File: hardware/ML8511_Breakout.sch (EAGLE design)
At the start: 9 parts, among them U1 ML8511-UV-SENSOR

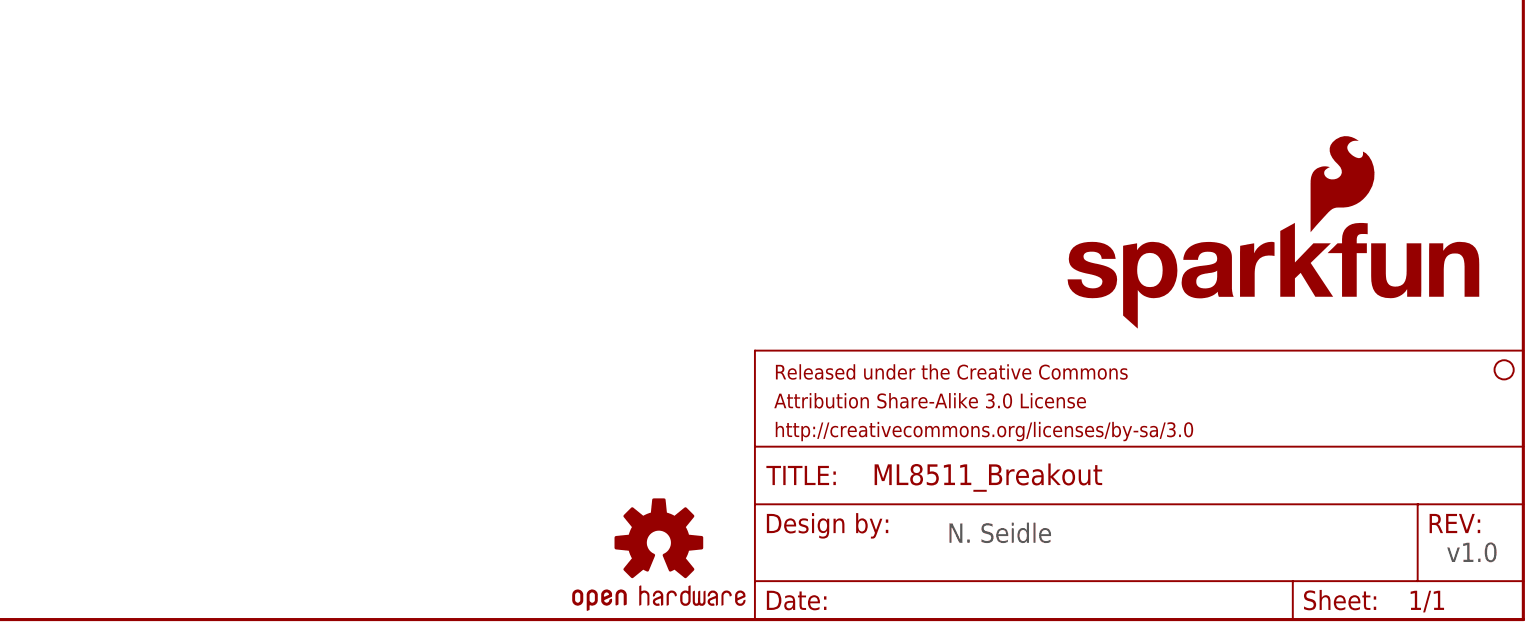
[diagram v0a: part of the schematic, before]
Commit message: DFM Changes
1.) Modified 3.3V trace so junction is not on IC pad
2.) Added trestrict under IC
3.) Routed GND trace directly away from IC
4.) Modified silk to better incorporate OSHW logo
5.) Version numbers between sch and brd are now consistent at v10
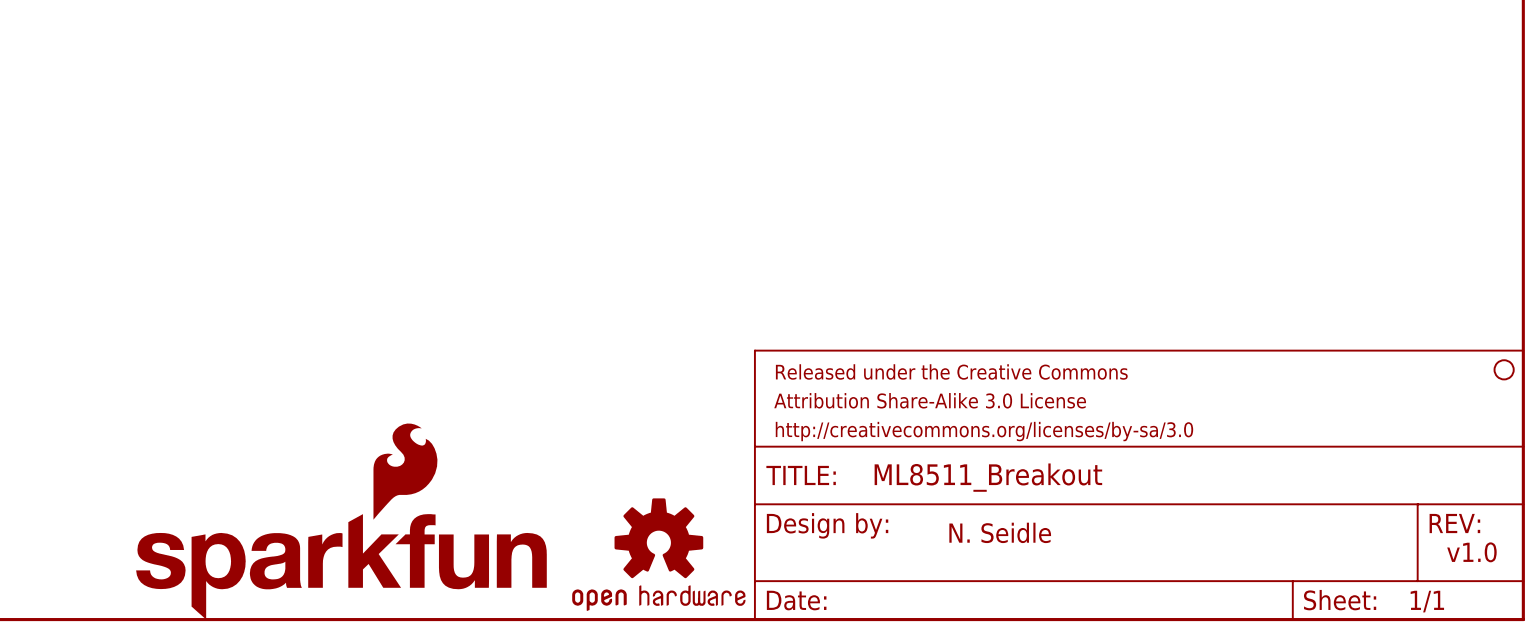
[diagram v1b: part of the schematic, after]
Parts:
- removed LOGO1: SFE_LOGO_NAME_FLAME.1_INCH, SparkFun-Aesthetics:SFE_LOGO_NAME_FLAME.1_INCH
- added LOGO3: SFE_LOGO_FLAME.1_INCH, SparkFun-Aesthetics:SFE_LOGO_FLAME.1_INCH
- added LOGO4: SFE_LOGO_NAME.1_INCH, SparkFun-Aesthetics:SFE_LOGO_NAME.1_INCH
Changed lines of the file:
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@@
 <grid distance="0.1" unitdist="inch" unit="inch" style="lines" multiple="1" display="no" altdistance="0.01" altunitdist="inch" altunit="inch"/>
 <layers>
-<layer number="1" name="Top" color="4" fill="1" visible="yes" active="no"/>
-<layer number="2" name="Route2" color="1" fill="3" visible="yes" active="no"/>
-<layer number="3" name="Route3" color="4" fill="3" visible="yes" active="no"/>
-<layer number="4" name="Route4" color="1" fill="4" visible="yes" active="no"/>
-<layer number="5" name="Route5" color="4" fill="4" visible="yes" active="no"/>
-<layer number="6" name="Route6" color="1" fill="8" visible="yes" active="no"/>
-<layer number="7" name="Route7" color="4" fill="8" visible="yes" active="no"/>
-<layer number="8" name="Route8" color="1" fill="2" visible="yes" active="no"/>
-<layer number="9" name="Route9" color="4" fill="2" visible="yes" active="no"/>
-<layer number="10" name="Route10" color="1" fill="7" visible="yes" active="no"/>
-<layer number="11" name="Route11" color="4" fill="7" visible="yes" active="no"/>
-<layer number="12" name="Route12" color="1" fill="5" visible="yes" active="no"/>
-<layer number="13" name="Route13" color="4" fill="5" visible="yes" active="no"/>
-<layer number="14" name="Route14" color="1" fill="6" visible="yes" active="no"/>
-<layer number="15" name="Route15" color="4" fill="6" visible="yes" active="no"/>
-<layer number="16" name="Bottom" color="1" fill="1" visible="yes" active="no"/>
-<layer number="17" name="Pads" color="2" fill="1" visible="yes" active="no"/>
-<layer number="18" name="Vias" color="2" fill="1" visible="yes" active="no"/>
-<layer number="19" name="Unrouted" color="14" fill="1" visible="yes" active="no"/>
-<layer number="20" name="Dimension" color="15" fill="1" visible="yes" active="no"/>
-<layer number="21" name="tPlace" color="16" fill="1" visible="yes" active="no"/>
-<layer number="22" name="bPlace" color="14" fill="1" visible="yes" active="no"/>
-<layer number="23" name="tOrigins" color="15" fill="1" visible="yes" active="no"/>
-<layer number="24" name="bOrigins" color="15" fill="1" visible="yes" active="no"/>
-<layer number="25" name="tNames" color="7" fill="1" visible="yes" active="no"/>
-<layer number="26" name="bNames" color="7" fill="1" visible="yes" active="no"/>
-<layer number="27" name="tValues" color="7" fill="1" visible="yes" active="no"/>
-<layer number="28" name="bValues" color="7" fill="1" visible="yes" active="no"/>
+<layer number="1" name="Top" color="4" fill="1" visible="no" active="no"/>
+<layer number="2" name="Route2" color="1" fill="3" visible="no" active="no"/>
+<layer number="3" name="Route3" color="4" fill="3" visible="no" active="no"/>
+<layer number="4" name="Route4" color="1" fill="4" visible="no" active="no"/>
+<layer number="5" name="Route5" color="4" fill="4" visible="no" active="no"/>
+<layer number="6" name="Route6" color="1" fill="8" visible="no" active="no"/>
+<layer number="7" name="Route7" color="4" fill="8" visible="no" active="no"/>
+<layer number="8" name="Route8" color="1" fill="2" visible="no" active="no"/>
+<layer number="9" name="Route9" color="4" fill="2" visible="no" active="no"/>
+<layer number="10" name="Route10" color="1" fill="7" visible="no" active="no"/>
+<layer number="11" name="Route11" color="4" fill="7" visible="no" active="no"/>
+<layer number="12" name="Route12" color="1" fill="5" visible="no" active="no"/>
+<layer number="13" name="Route13" color="4" fill="5" visible="no" active="no"/>
+<layer number="14" name="Route14" color="1" fill="6" visible="no" active="no"/>
+<layer number="15" name="Route15" color="4" fill="6" visible="no" active="no"/>
+<layer number="16" name="Bottom" color="1" fill="1" visible="no" active="no"/>
+<layer number="17" name="Pads" color="2" fill="1" visible="no" active="no"/>
+<layer number="18" name="Vias" color="2" fill="1" visible="no" active="no"/>
+<layer number="19" name="Unrouted" color="14" fill="1" visible="no" active="no"/>
+<layer number="20" name="Dimension" color="15" fill="1" visible="no" active="no"/>
+<layer number="21" name="tPlace" color="16" fill="1" visible="no" active="no"/>
+<layer number="22" name="bPlace" color="14" fill="1" visible="no" active="no"/>
+<layer number="23" name="tOrigins" color="15" fill="1" visible="no" active="no"/>
+<layer number="24" name="bOrigins" color="15" fill="1" visible="no" active="no"/>
+<layer number="25" name="tNames" color="7" fill="1" visible="no" active="no"/>
+<layer number="26" name="bNames" color="7" fill="1" visible="no" active="no"/>
+<layer number="27" name="tValues" color="7" fill="1" visible="no" active="no"/>
+<layer number="28" name="bValues" color="7" fill="1" visible="no" active="no"/>
 <layer number="29" name="tStop" color="7" fill="3" visible="no" active="no"/>
 <layer number="30" name="bStop" color="7" fill="6" visible="no" active="no"/>
@@
 <layer number="35" name="tGlue" color="7" fill="4" visible="no" active="no"/>
 <layer number="36" name="bGlue" color="7" fill="5" visible="no" active="no"/>
-<layer number="37" name="tTest" color="7" fill="1" visible="yes" active="no"/>
-<layer number="38" name="bTest" color="7" fill="1" visible="yes" active="no"/>
+<layer number="37" name="tTest" color="7" fill="1" visible="no" active="no"/>
+<layer number="38" name="bTest" color="7" fill="1" visible="no" active="no"/>
 <layer number="39" name="tKeepout" color="4" fill="11" visible="no" active="no"/>
 <layer number="40" name="bKeepout" color="1" fill="11" visible="no" active="no"/>
@@
 <layer number="44" name="Drills" color="7" fill="1" visible="no" active="no"/>
 <layer number="45" name="Holes" color="7" fill="1" visible="no" active="no"/>
-<layer number="46" name="Milling" color="3" fill="1" visible="yes" active="no"/>
-<layer number="47" name="Measures" color="7" fill="1" visible="yes" active="no"/>
-<layer number="48" name="Document" color="7" fill="1" visible="yes" active="no"/>
-<layer number="49" name="Reference" color="7" fill="1" visible="yes" active="no"/>
-<layer number="50" name="dxf" color="7" fill="1" visible="yes" active="no"/>
-<layer number="51" name="tDocu" color="6" fill="1" visible="yes" active="no"/>
-<layer number="52" name="bDocu" color="7" fill="1" visible="yes" active="no"/>
-<layer number="53" name="tGND_GNDA" color="7" fill="9" visible="yes" active="no"/>
-<layer number="54" name="bGND_GNDA" color="1" fill="9" visible="yes" active="no"/>
-<layer number="56" name="wert" color="7" fill="1" visible="yes" active="no"/>
+<layer number="46" name="Milling" color="3" fill="1" visible="no" active="no"/>
+<layer number="47" name="Measures" color="7" fill="1" visible="no" active="no"/>
+<layer number="48" name="Document" color="7" fill="1" visible="no" active="no"/>
+<layer number="49" name="Reference" color="7" fill="1" visible="no" active="no"/>
+<layer number="50" name="dxf" color="7" fill="1" visible="no" active="no"/>
+<layer number="51" name="tDocu" color="6" fill="1" visible="no" active="no"/>
+<layer number="52" name="bDocu" color="7" fill="1" visible="no" active="no"/>
+<layer number="53" name="tGND_GNDA" color="7" fill="9" visible="no" active="no"/>
+<layer number="54" name="bGND_GNDA" color="1" fill="9" visible="no" active="no"/>
+<layer number="56" name="wert" color="7" fill="1" visible="no" active="no"/>
 <layer number="91" name="Nets" color="2" fill="1" visible="yes" active="yes"/>
 <layer number="92" name="Busses" color="1" fill="1" visible="yes" active="yes"/>
@@
 <part name="R1" library="SparkFun-Resistors" deviceset="10KOHM1/10W1%(0603)" device="0603" value="10K"/>
 <part name="SUPPLY4" library="SparkFun-Aesthetics" deviceset="3.3V" device=""/>
-<part name="LOGO1" library="SparkFun-Aesthetics" deviceset="SFE_LOGO_NAME_FLAME" device=".1_INCH"/>
 <part name="LOGO2" library="SparkFun-Aesthetics" deviceset="OSHW-LOGO" device="S" value="OSHW-LOGOS"/>
+<part name="LOGO3" library="SparkFun-Aesthetics" deviceset="SFE_LOGO_FLAME" device=".1_INCH"/>
+<part name="LOGO4" library="SparkFun-Aesthetics" deviceset="SFE_LOGO_NAME" device=".1_INCH"/>
 </parts>
 <sheets>
 <sheet>
 <plain>
-<text x="172.72" y="10.16" size="2.54" layer="97">N. Seidle</text>
-<text x="238.76" y="7.62" size="2.54" layer="97">v1.0</text>
+<text x="172.72" y="10.16" size="2.54" layer="94">N. Seidle</text>
+<text x="238.76" y="7.62" size="2.54" layer="94">v1.0</text>
 </plain>
 <instances>
@@
 <instance part="R1" gate="G$1" x="137.16" y="134.62" rot="R90"/>
 <instance part="SUPPLY4" gate="G$1" x="137.16" y="142.24"/>
-<instance part="LOGO1" gate="G$1" x="187.96" y="38.1"/>
 <instance part="LOGO2" gate="G$1" x="134.62" y="10.16"/>
+<instance part="LOGO3" gate="G$1" x="96.52" y="12.7"/>
+<instance part="LOGO4" gate="G$1" x="63.5" y="0"/>
 </instances>
 <busses>

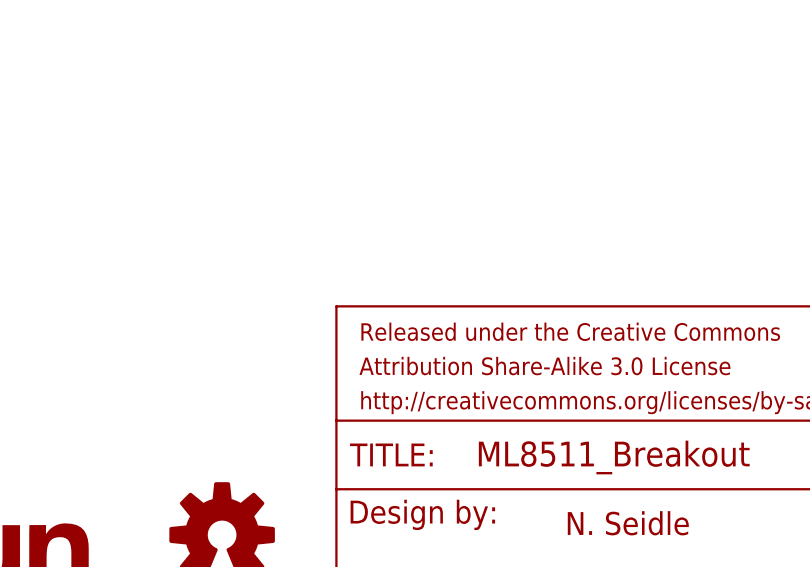
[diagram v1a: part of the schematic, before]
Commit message: added local fiducials
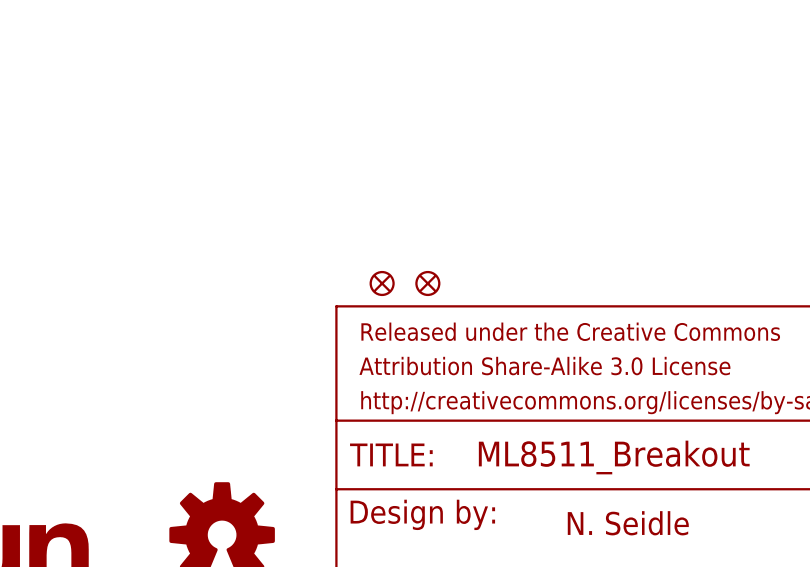
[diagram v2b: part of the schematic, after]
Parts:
- added FID1, FID2: FIDUCIAL1X2, SparkFun-Aesthetics:FIDUCIAL1X2
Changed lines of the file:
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@@
 <part name="LOGO3" library="SparkFun-Aesthetics" deviceset="SFE_LOGO_FLAME" device=".1_INCH"/>
 <part name="LOGO4" library="SparkFun-Aesthetics" deviceset="SFE_LOGO_NAME" device=".1_INCH"/>
+<part name="FID1" library="SparkFun-Aesthetics" deviceset="FIDUCIAL" device="1X2"/>
+<part name="FID2" library="SparkFun-Aesthetics" deviceset="FIDUCIAL" device="1X2"/>
 </parts>
 <sheets>
@@
 <instance part="LOGO3" gate="G$1" x="96.52" y="12.7"/>
 <instance part="LOGO4" gate="G$1" x="63.5" y="0"/>
+<instance part="FID1" gate="G$1" x="152.4" y="38.1"/>
+<instance part="FID2" gate="G$1" x="157.48" y="38.1"/>
 </instances>
 <busses>
